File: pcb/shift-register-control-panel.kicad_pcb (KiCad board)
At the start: 2 copper layers, 65.2 x 41.8 mm, 30 parts, among them J1 Conn_01x08, J2 USB_A, SW1 INPUT, SW2 SHIFT, SW3 CLEAR, SW4 DISPLAY, U1 74HC595, U2 LM7805_TO220

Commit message: updated gerbers
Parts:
- moved J2 3.03 mm to (181.0, 100.3)
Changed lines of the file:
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@@
 		(tags "LED")
 		(property "Reference" "D4"
-			(at 1.154061 4.129144 90)
+			(at 0.864061 3.979144 90)
 			(layer "F.SilkS")
 			(effects
@@
 		(tags "LED")
 		(property "Reference" "D5"
-			(at 5.649061 0.676287 90)
+			(at 1.244061 3.95343 90)
 			(layer "F.SilkS")
-			(hide yes)
 			(effects
 				(font
@@
 			)
 		)
-		(property "Datasheet" "~"
+		(property "Datasheet" ""
 			(at 0 0 90)
 			(layer "F.Fab")
@@
 			)
 		)
-		(property "Description" "Light emitting diode"
+		(property "Description" ""
 			(at 0 0 90)
 			(layer "F.Fab")
@@
 	(footprint "Connector_USB:USB_A_Molex_67643_Horizontal"
 		(layer "F.Cu")
-		(at 180.95 97.32 90)
+		(at 181.01 100.35 90)
 		(descr "USB type A, Horizontal, https://www.molex.com/pdm_docs/sd/676433910_sd.pdf")
 		(tags "USB_A Female Connector receptacle")
@@
 	)
 	(segment
-		(start 173.69 97.32)
-		(end 172.3 98.71)
+		(start 178.2 100.35)
+		(end 176.56 98.71)
+		(width 0.2)
+		(layer "F.Cu")
+		(net 13)
+	)
+	(segment
+		(start 181.01 100.35)
+		(end 178.2 100.35)
 		(width 0.2)
 		(layer "F.Cu")
@@
 	)
 	(segment
-		(start 180.95 97.32)
-		(end 173.69 97.32)
+		(start 176.56 98.71)
+		(end 172.3 98.71)
 		(width 0.2)
 		(layer "F.Cu")

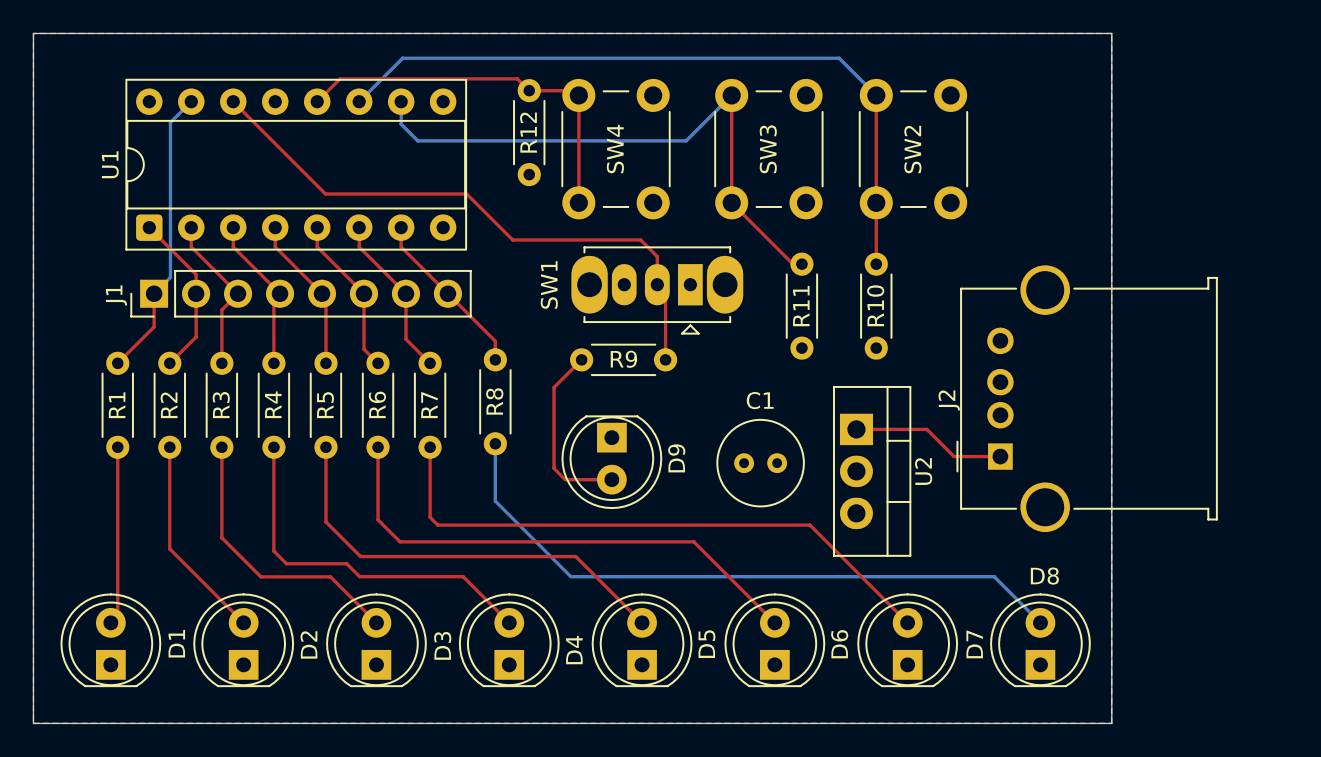
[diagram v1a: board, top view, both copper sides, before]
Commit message: added debounce to shift input
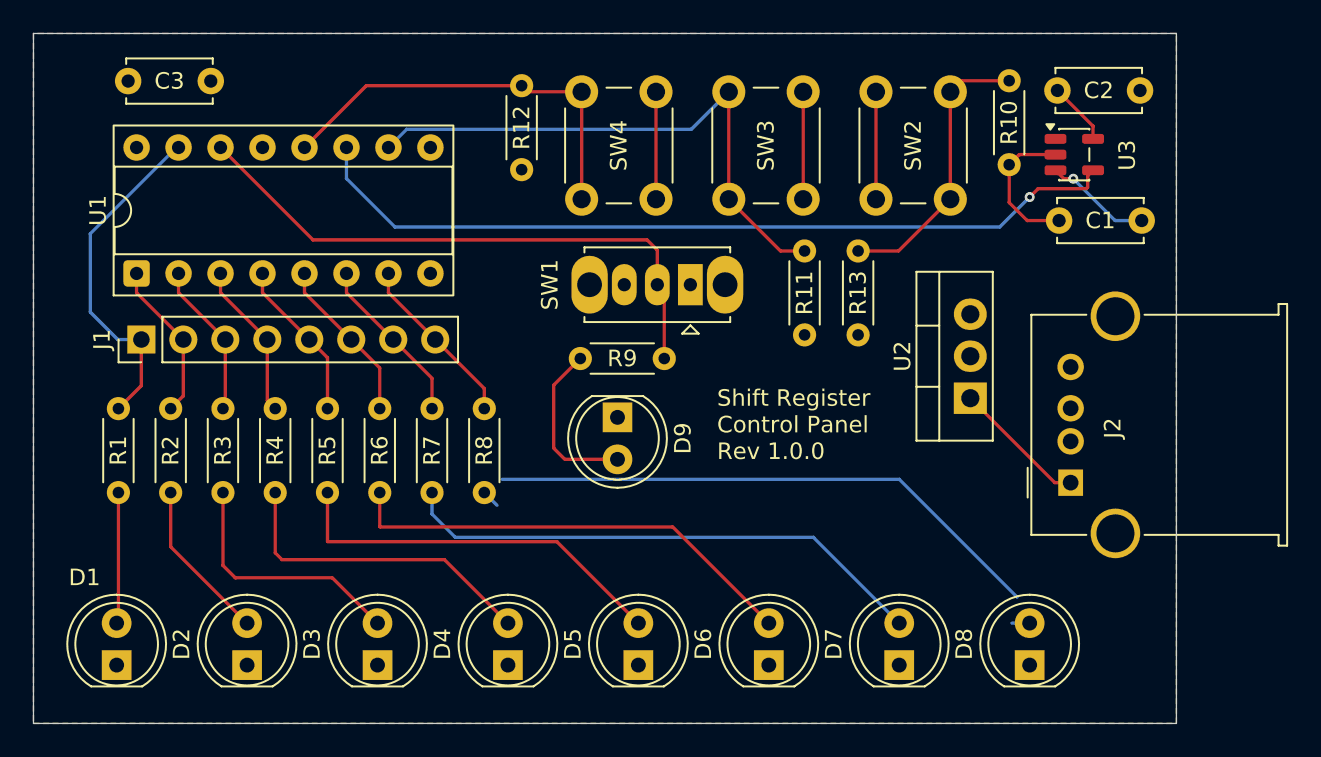
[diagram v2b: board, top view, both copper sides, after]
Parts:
- added C2: 100 nF, Capacitor_THT:C_Disc_D5.0mm_W2.5mm_P5.00mm, F.Cu at (189.5, 78.2)
- added C3: 100 nF, Capacitor_THT:C_Disc_D5.0mm_W2.5mm_P5.00mm, F.Cu at (133.2, 77.6)
- added R13: 5k, Resistor_THT:R_Axial_DIN0204_L3.6mm_D1.6mm_P5.08mm_Horizontal, F.Cu at (172.4, 87.9)
- added U3: SN74LVC1G14, Package_TO_SOT_SMD:SOT-23-5, F.Cu at (185.5, 82.1)
- C1: value 0.1 µF -> 100 nF; footprint Capacitor_THT:C_Radial_D5.0mm_H7.0mm_P2.00mm -> Capacitor_THT:C_Disc_D5.0mm_W2.5mm_P5.00mm
- D1: value OUT1 -> RED
- D2: value OUT2 -> RED
- D3: value OUT3 -> RED
- D4: value OUT4 -> RED
- D5: value OUT5 -> RED
- D6: value OUT6 -> RED
- D7: value OUT7 -> RED
- D8: value OUT8 -> RED
- D9: value LED -> INPUT_STATUS
- R1, R2, R3, R4, R5, R6, R7, R8: value 330Ω -> 1kΩ
- R10: value 10 kΩ -> 1k
- moved C1 24.1 mm to (184.6, 86.1)
- moved R10 13.7 mm to (181.5, 77.6)
- moved SW2 7.74 mm to (173.5, 84.8), turned to 90 degrees
- moved U2 7.14 mm to (179.2, 96.8), turned to 90 degrees
- moved J2 4.53 mm to (185.3, 101.9)
- moved R8 3.03 mm to (149.8, 97.5)
- moved J1 2.88 mm to (129.0, 93.3)
- moved U1 2.88 mm to (128.7, 89.3)
- moved R7 2.74 mm to (146.6, 97.5)
- moved R6 2.74 mm to (143.5, 97.5)
- moved R5 2.74 mm to (140.3, 97.5)
- moved R4 2.74 mm to (137.1, 97.5)
- moved R3 2.74 mm to (134.0, 97.5)
- moved R2 2.74 mm to (130.8, 97.5)
- moved R1 2.74 mm to (127.6, 97.5)
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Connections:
- C1 pad 1: GND -> Net-(C1-Pad1)
- C1 pad 2: +5V -> GND
- R10 pad 1: Net-(U1-SRCLK) -> Net-(R10-Pad1)
- R10 pad 2: GND -> Net-(C1-Pad1)
- SW2 pad 1: +5V -> GND
- SW2 pad 2: Net-(U1-SRCLK) -> Net-(R10-Pad1)
- U1 pad 13: +5V -> GND
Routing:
- net GND: track 0.00 -> 19.5 mm, vias 0 -> 1
- net Net-(R10-Pad1): track 0.00 -> 17.2 mm
- net +5V: track 0.00 -> 10.3 mm
- net Net-(C1-Pad1): track 0.00 -> 8.82 mm
- net Net-(U1-SRCLK): track 43.5 -> 50.1 mm, vias 0 -> 1
- net Net-(D7-A): track 35.8 -> 32.3 mm
- net Net-(D8-A): track 39.5 -> 36.3 mm
- net /OUT1: track 17.7 -> 20.8 mm
- net Net-(D6-A): track 31.0 -> 28.0 mm
- net Net-(D1-A): track 10.8 -> 7.94 mm
- net Net-(D4-A): track 22.3 -> 19.5 mm
- net Net-(D2-A): track 12.5 -> 9.81 mm
- net Net-(D5-A): track 26.2 -> 23.8 mm
- net Net-(D3-A): track 17.0 -> 15.2 mm
- net Net-(U1-RCLK): track 23.3 -> 25.0 mm
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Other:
- board size 65.2 x 41.8 mm -> 69.2 x 41.8 mm
- board text added: "Shift Register Control Panel Rev 1.0.0"
